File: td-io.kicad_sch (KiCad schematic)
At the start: 17 parts, among them J1 Conn_02x10_Odd_Even, J2 USB_B, J3 Conn_01x03, J4 Conn_01x02, J5 I2C, J6 DIPS, Q1 AO4818B, U1 Pico, U2 ISL3175EIBZ-T

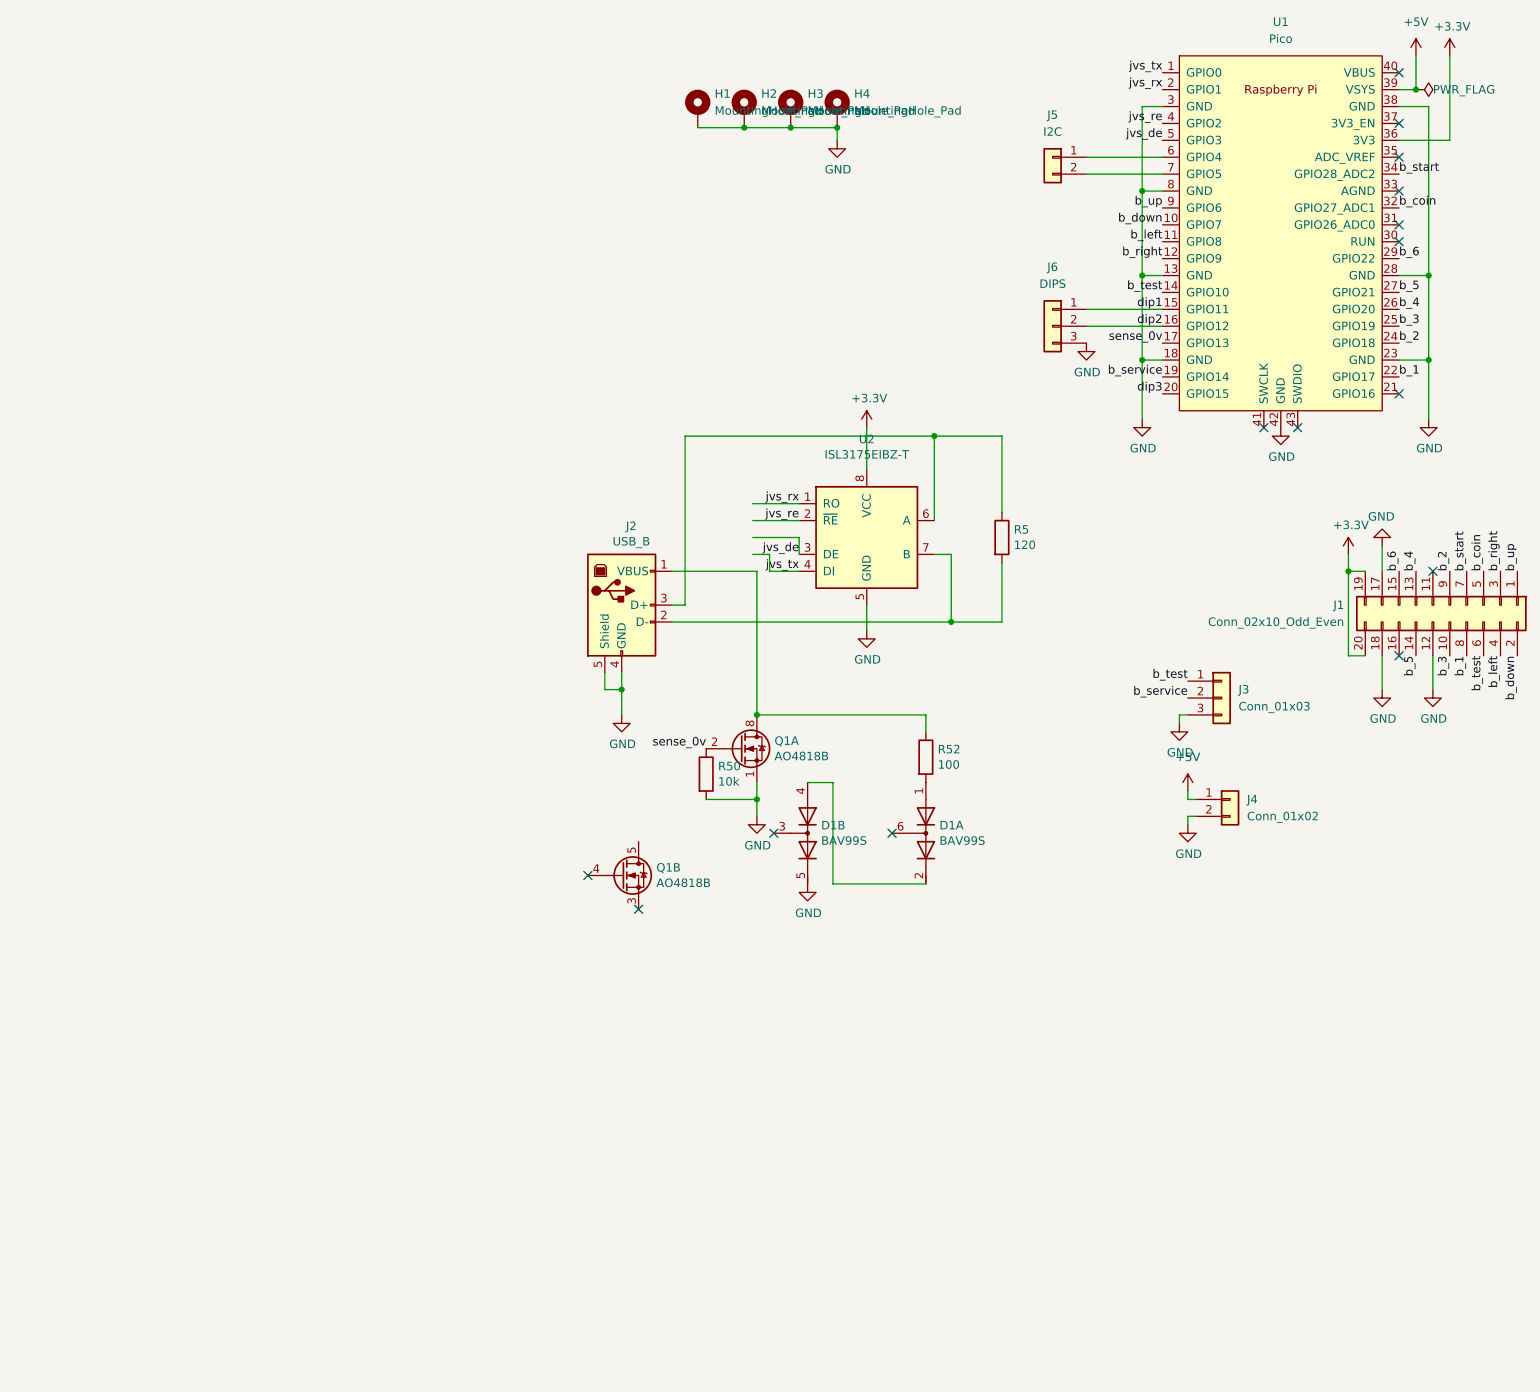
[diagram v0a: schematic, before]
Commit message: Cleaned up pcb
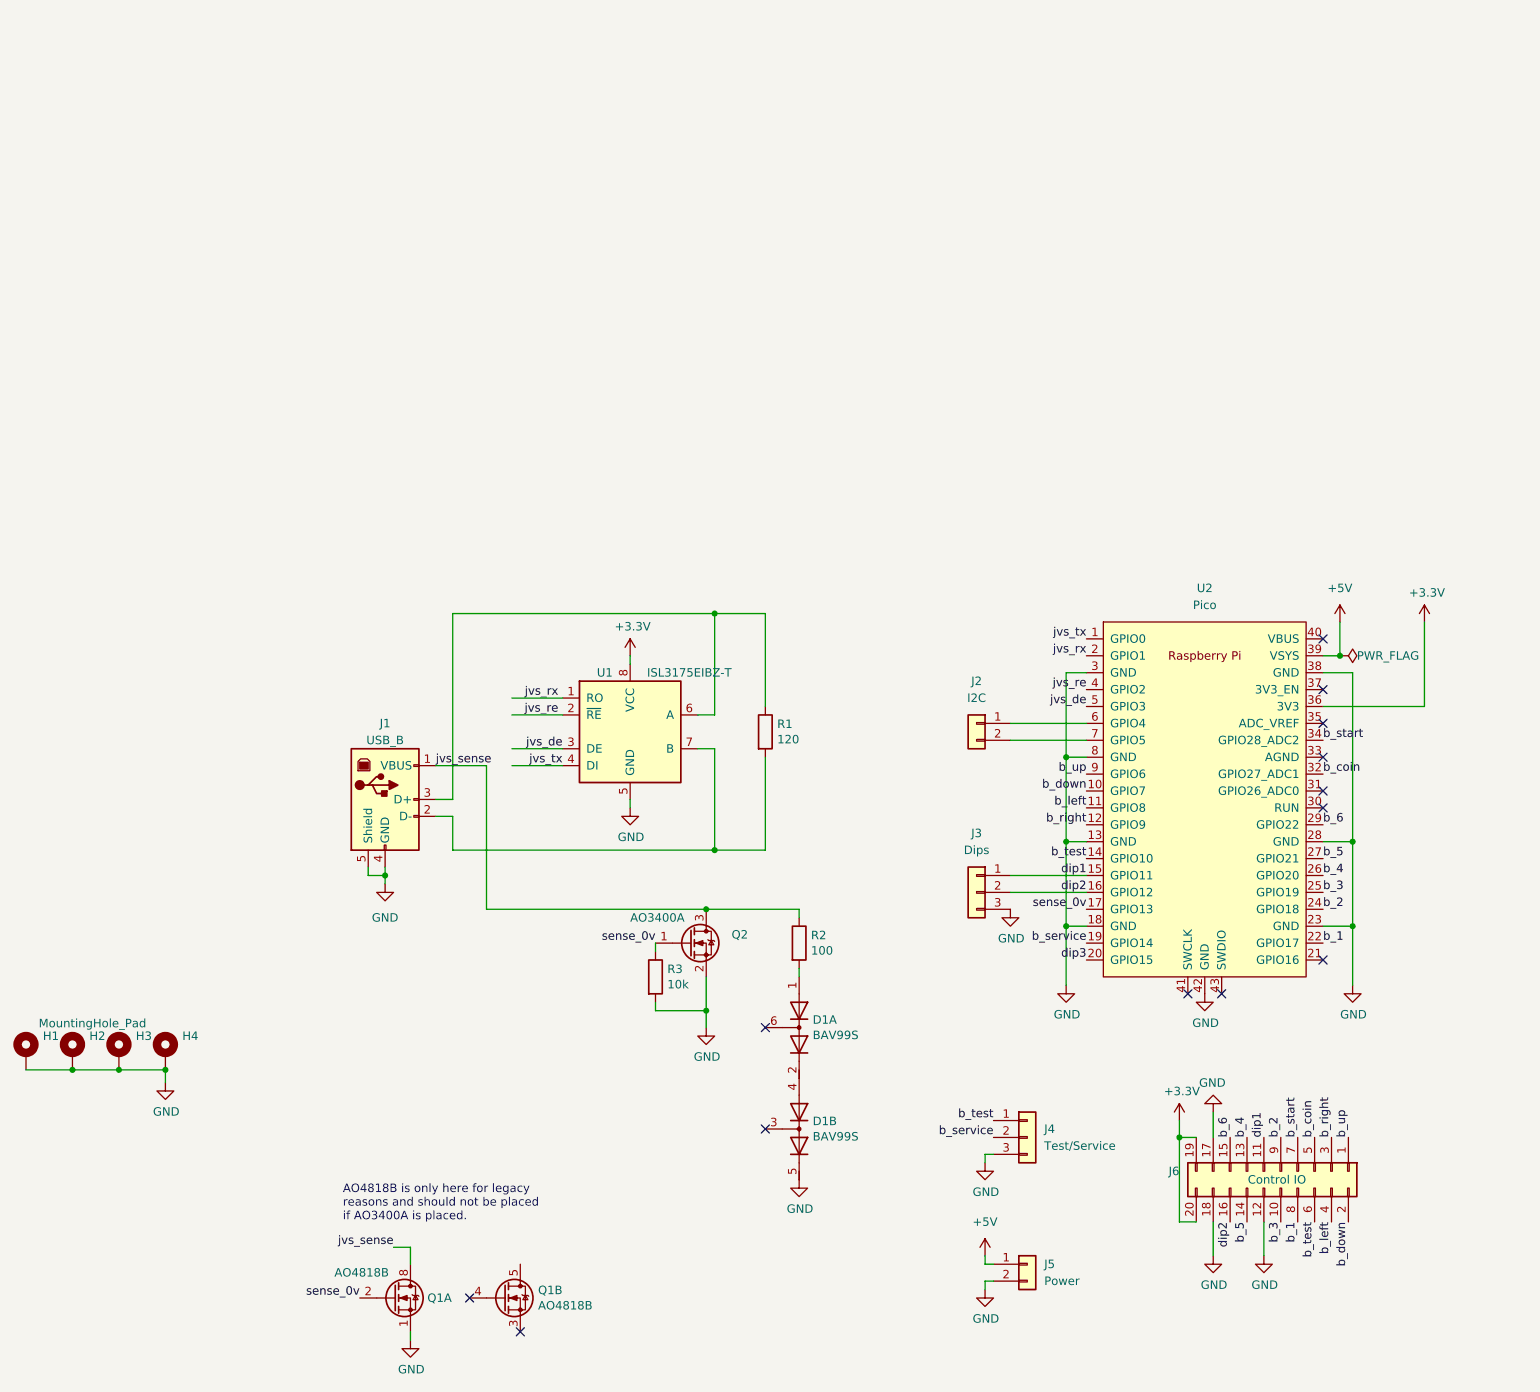
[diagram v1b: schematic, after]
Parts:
- added Q2: AO3400A, Package_TO_SOT_SMD:SOT-23, symbol Transistor_FET:AO3400A
- J3: renamed from J6; value DIPS -> Dips
- J4: renamed from J3; value Conn_01x03 -> Test/Service
- J5: renamed from J4; value Conn_01x02 -> Power
- J6: renamed from J1; value Conn_02x10_Odd_Even -> Control IO
- renumbered J2 to J1, J5 to J2, R5 to R1, R52 to R2, R50 to R3, U2 to U1, U1 to U2
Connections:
- net GND: now also Q2.2 (S)
- net dip1: now also J6.11 (Pin_11)
- net dip2: now also J6.16 (Pin_16)
- net sense_0v: now also Q2.1 (G)
- net jvs_sense: now reaches J1.1 (VBUS), Q1.7 (D1), Q1.8 (D1), R2.1
- net jvs_sense: now also Q2.3 (D)
- no-connect marks 15 -> 13
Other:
- note added: "AO4818B is only here for legacy reasons and should not be placed if AO3400A is placed."
- moved on the sheet: D1A, D1B, H1, H2, H3, H4, J1, J2, J3, J4, J5, J6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
